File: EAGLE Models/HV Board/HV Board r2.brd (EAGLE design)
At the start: 106.7 x 62.2 mm, 27 parts, among them K1 HE751, U1 G2RL-1-E, U2 CNY17-3, U3 MJD45H11T4G, U4 MMBT4401-7-F

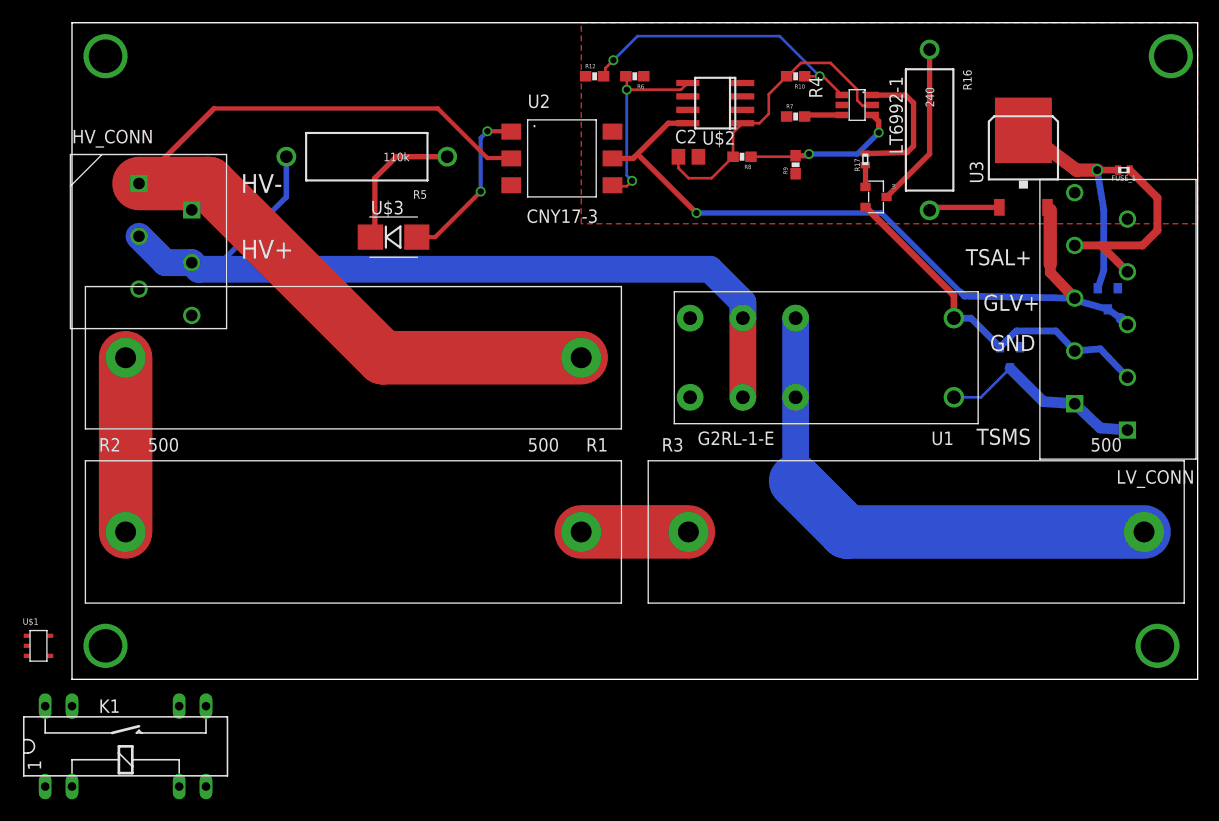
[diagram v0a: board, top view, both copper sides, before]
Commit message: Changed HV board for putting in line with MC
Integrated Discharge and TSAL circuit into one smaller board to put in a
box in line with the motor controller.
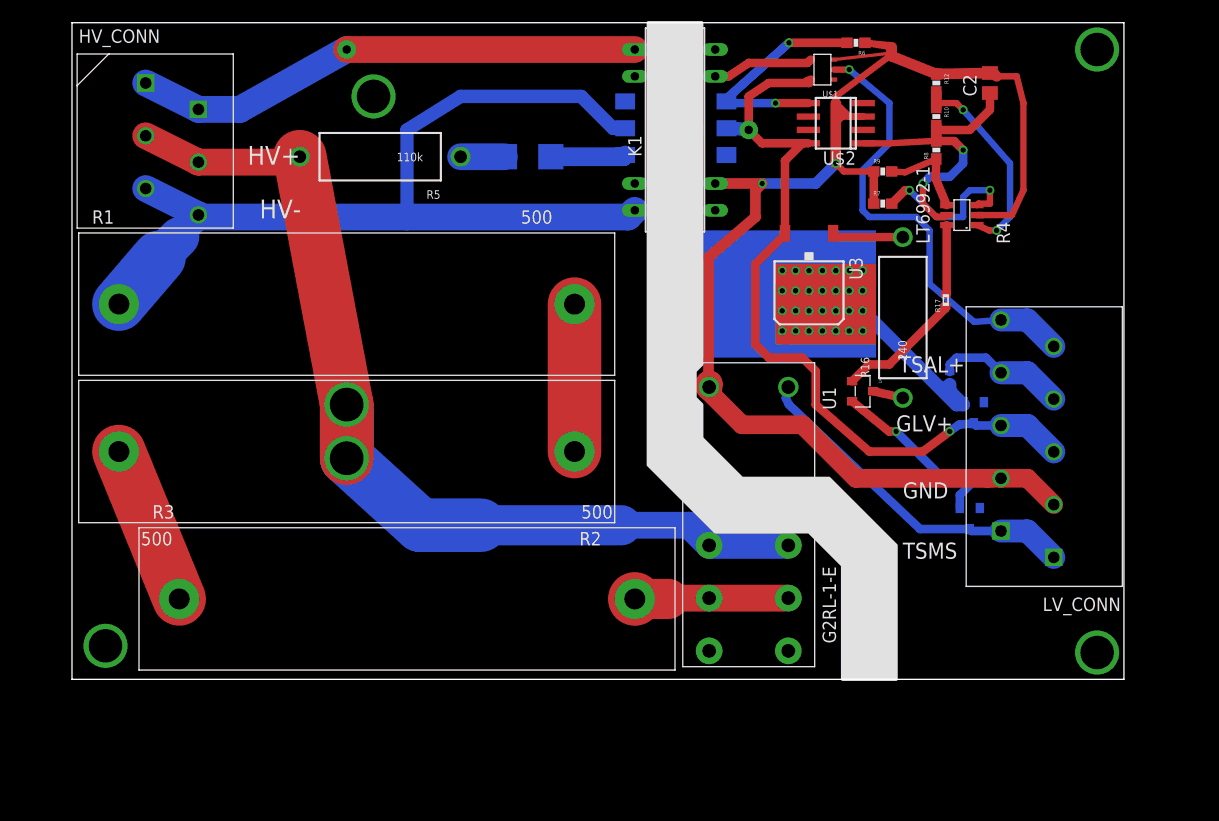
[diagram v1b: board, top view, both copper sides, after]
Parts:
- moved U$1 92.2 mm to (71.1, 57.8), turned to 180 degrees
- moved K1 78.3 mm to (57.1, 52.1), turned to 90 degrees
- moved R3 48.7 mm to (31.8, 7.62)
- moved R12 32.4 mm to (81.9, 56.5), turned to 270 degrees
- moved C2 29.4 mm to (87.0, 56.5), turned to 90 degrees
- moved FUSE_1 25.7 mm to (83.2, 28.6), flipped to the bottom, turned to 270 degrees
- moved U3 23.6 mm to (69.8, 37.5), turned to 180 degrees
- moved R6 21.2 mm to (74.3, 60.3)
- moved U4 18.5 mm to (74.9, 27.3)
- moved R8 18.4 mm to (81.9, 50.2), turned to 90 degrees
- moved U1 18.3 mm to (64.1, 12.7), turned to 270 degrees
- moved R16 18.0 mm to (78.7, 34.3), turned to 90 degrees
- moved R4 17.6 mm to (85.1, 42.5), turned to 90 degrees
- moved D2 16.7 mm to (85.5, 25.3)
- moved D1 15.7 mm to (85.1, 15.2)
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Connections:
- net GATE_IN: now also HV_CONN.1, HV_CONN.2; no longer HV_CONN.5, HV_CONN.6
- net HV+: now also U1.P$2, U1.P$7; no longer U1.P$3, U1.P$6
- net HV-: now also HV_CONN.5, HV_CONN.6; no longer HV_CONN.1, HV_CONN.2
- net N$3: now also U1.P$3, U1.P$6; no longer U1.P$2, U1.P$7
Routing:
- net GND: track 34.2 -> 166.5 mm, vias 0 -> 3
- net GATE_IN: track 0.00 -> 48.4 mm, vias 0 -> 1
- net POS_AIR: track 0.00 -> 44.0 mm, vias 0 -> 1
- net N$3: track 50.5 -> 14.6 mm
- net N$29: track 21.6 -> 52.1 mm, vias 1 -> 4
- net TSMS_IN: track 19.8 -> 32.7 mm
- net N$20: track 15.7 -> 2.88 mm
- net N$26: track 18.4 -> 30.4 mm
- net N$18: track 3.59 -> 15.6 mm, vias 0 -> 2
- net HV+: track 84.2 -> 95.0 mm, vias 0 -> 1
- net N$21: track 2.06 -> 12.0 mm
- net N$1: track 14.0 -> 4.15 mm
- net N$2: track 0.00 -> 9.58 mm
- net N$15: track 16.1 -> 7.11 mm, vias 2 -> 0
- net N$14: track 28.4 -> 19.8 mm
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- removed copper zone on layer 1, net GND
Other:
- board size 106.7 x 62.2 mm -> 99.7 x 62.2 mm
- board text added: "Formula Electric 2016: HV Board Schematic By: Thomas Willson Layout By: Michael DeLay thomas.willson@me.com miked2114@gmail.com"
- board text removed: "Formula Electric 2015: HV Board Designed By: Thomas Willson thomas.willson@me.com"
